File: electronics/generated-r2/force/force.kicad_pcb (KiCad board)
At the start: 2 copper layers, 18 x 12 mm, 7 parts, among them J1 HALL_3V3_GND_OUT, U1 DRV5055A3DBZR

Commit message: build(r2): publish final routed electronics and checks [skip ci]
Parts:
- U1: value DRV5055A3DBZR -> DRV5055A3QDBZR

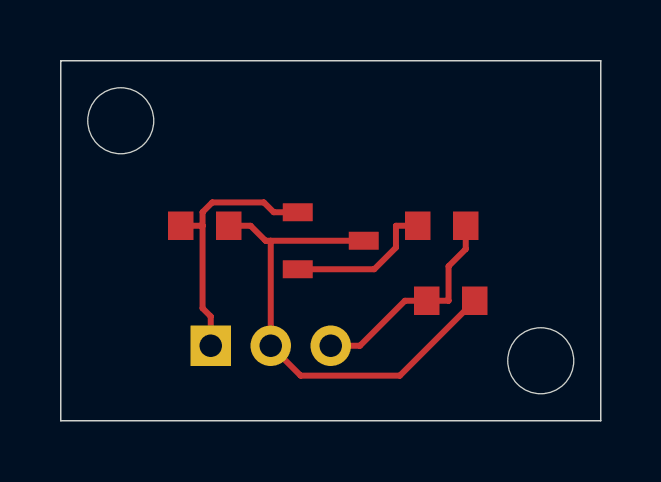
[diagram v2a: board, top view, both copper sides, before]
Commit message: build(r2): publish verified four-board electronics baseline [skip ci]
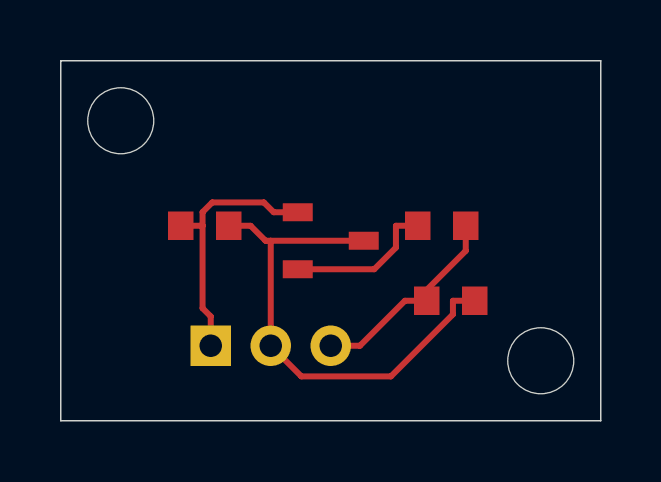
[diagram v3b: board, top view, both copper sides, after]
